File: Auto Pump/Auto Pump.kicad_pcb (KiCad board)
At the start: 2 copper layers, 15 parts, among them J1 12V Supply, J2 5V Supply, J3 Float High, J4 Float Low, J5 Manual Pump, J6 Pump, J7 12V Supply, Q1 PN2222A, U1 WeMos_D1_mini

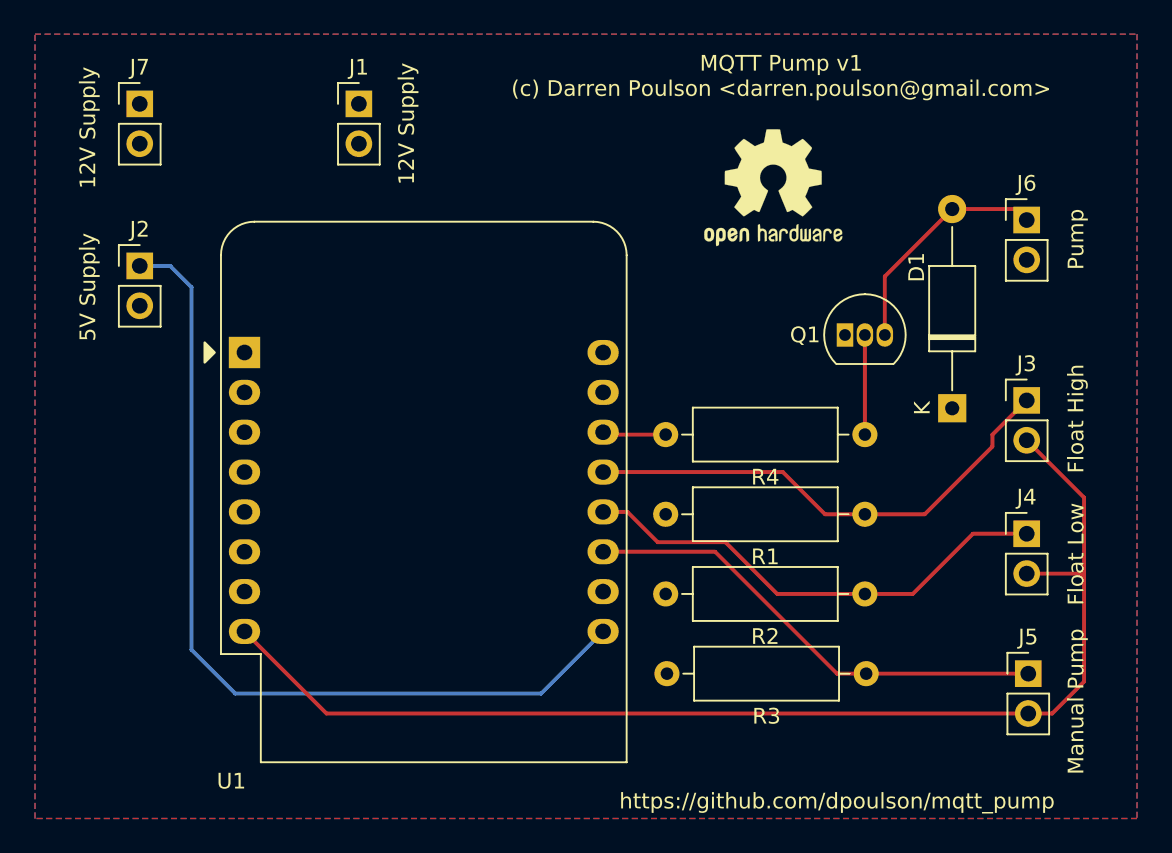
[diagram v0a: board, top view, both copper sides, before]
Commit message: First pass at arduino code using Homie standard
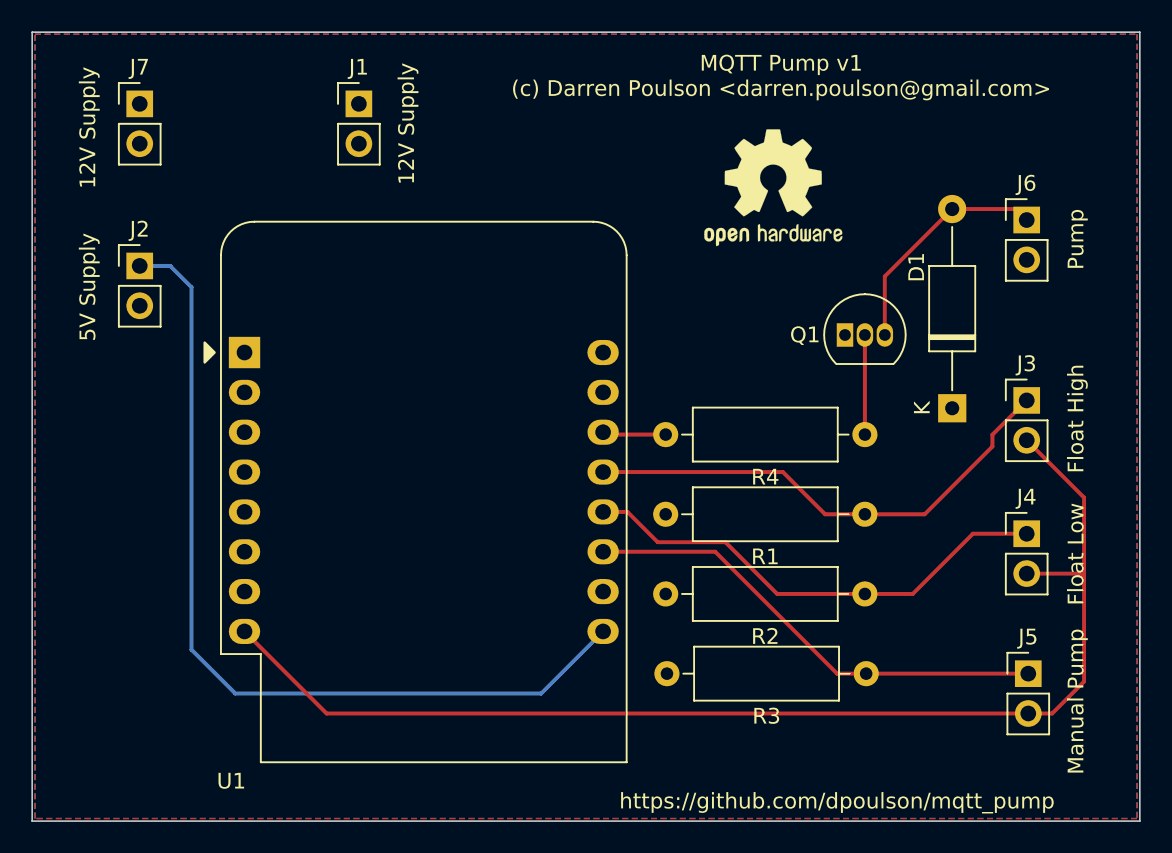
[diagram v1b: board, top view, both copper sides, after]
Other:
- board outline added: 70.6 x 50.3 mm
